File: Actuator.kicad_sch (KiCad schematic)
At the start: 2 parts, among them U4 DRV8833PWPR, U6 DRV8833PWPR

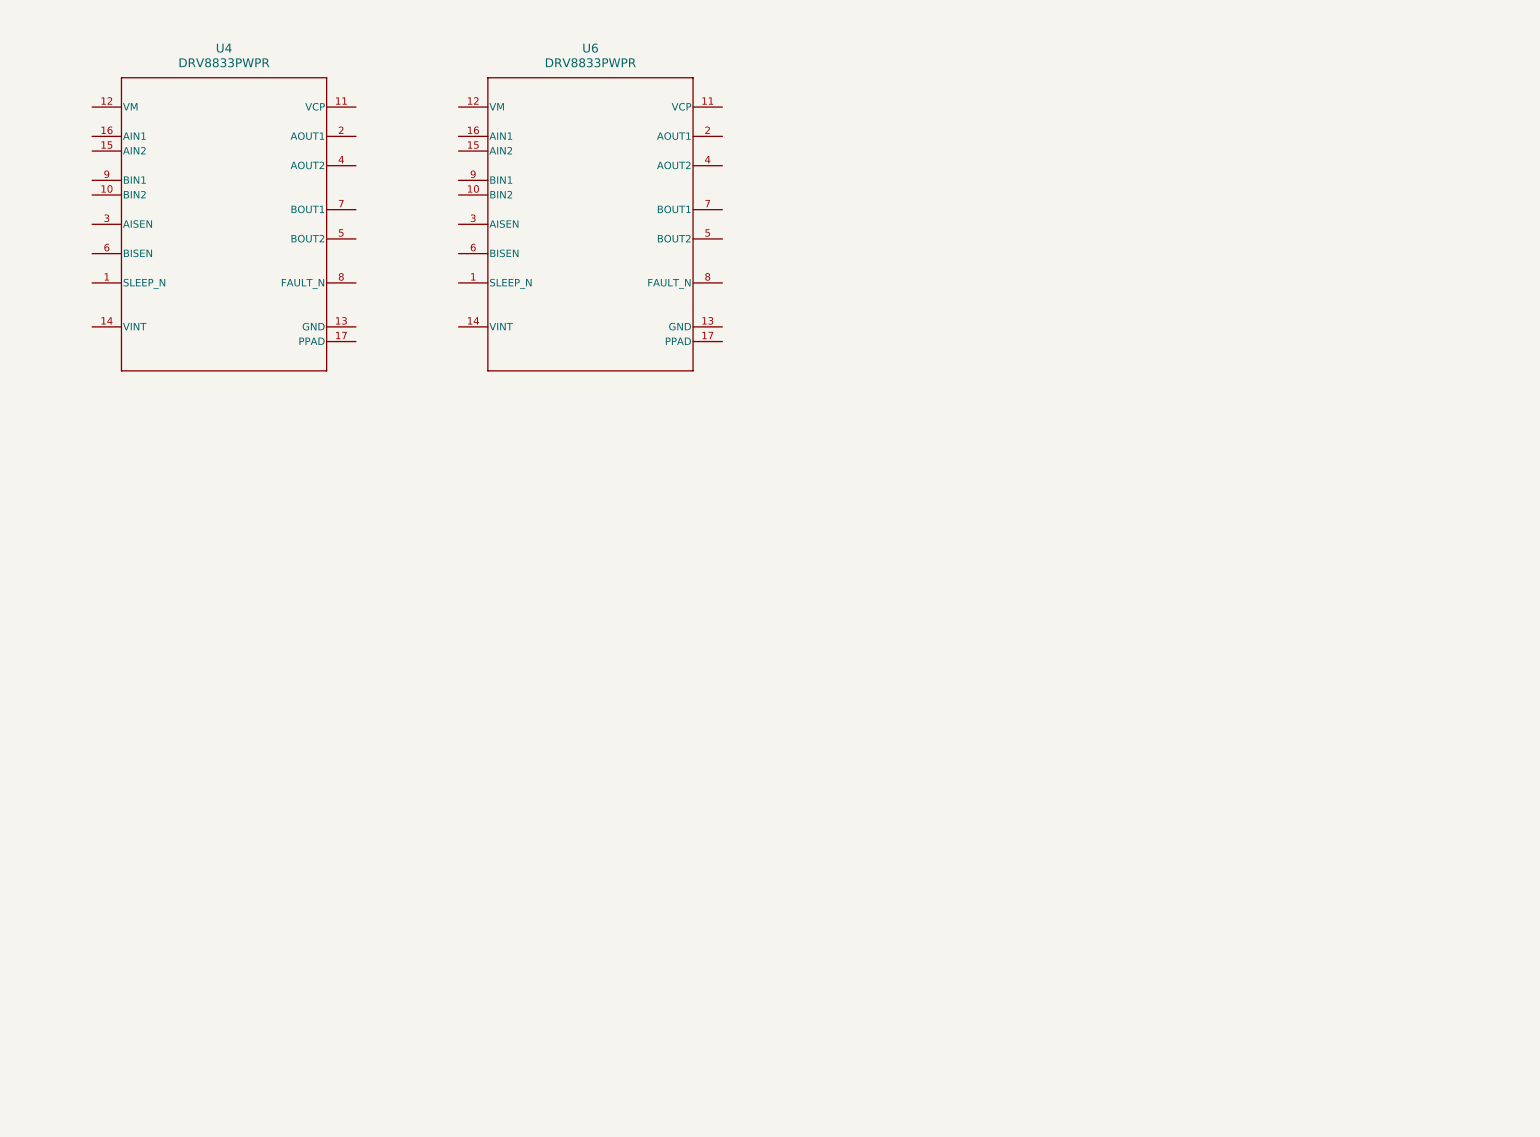
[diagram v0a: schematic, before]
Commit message: Added actuation circuit for x, y, and z axes
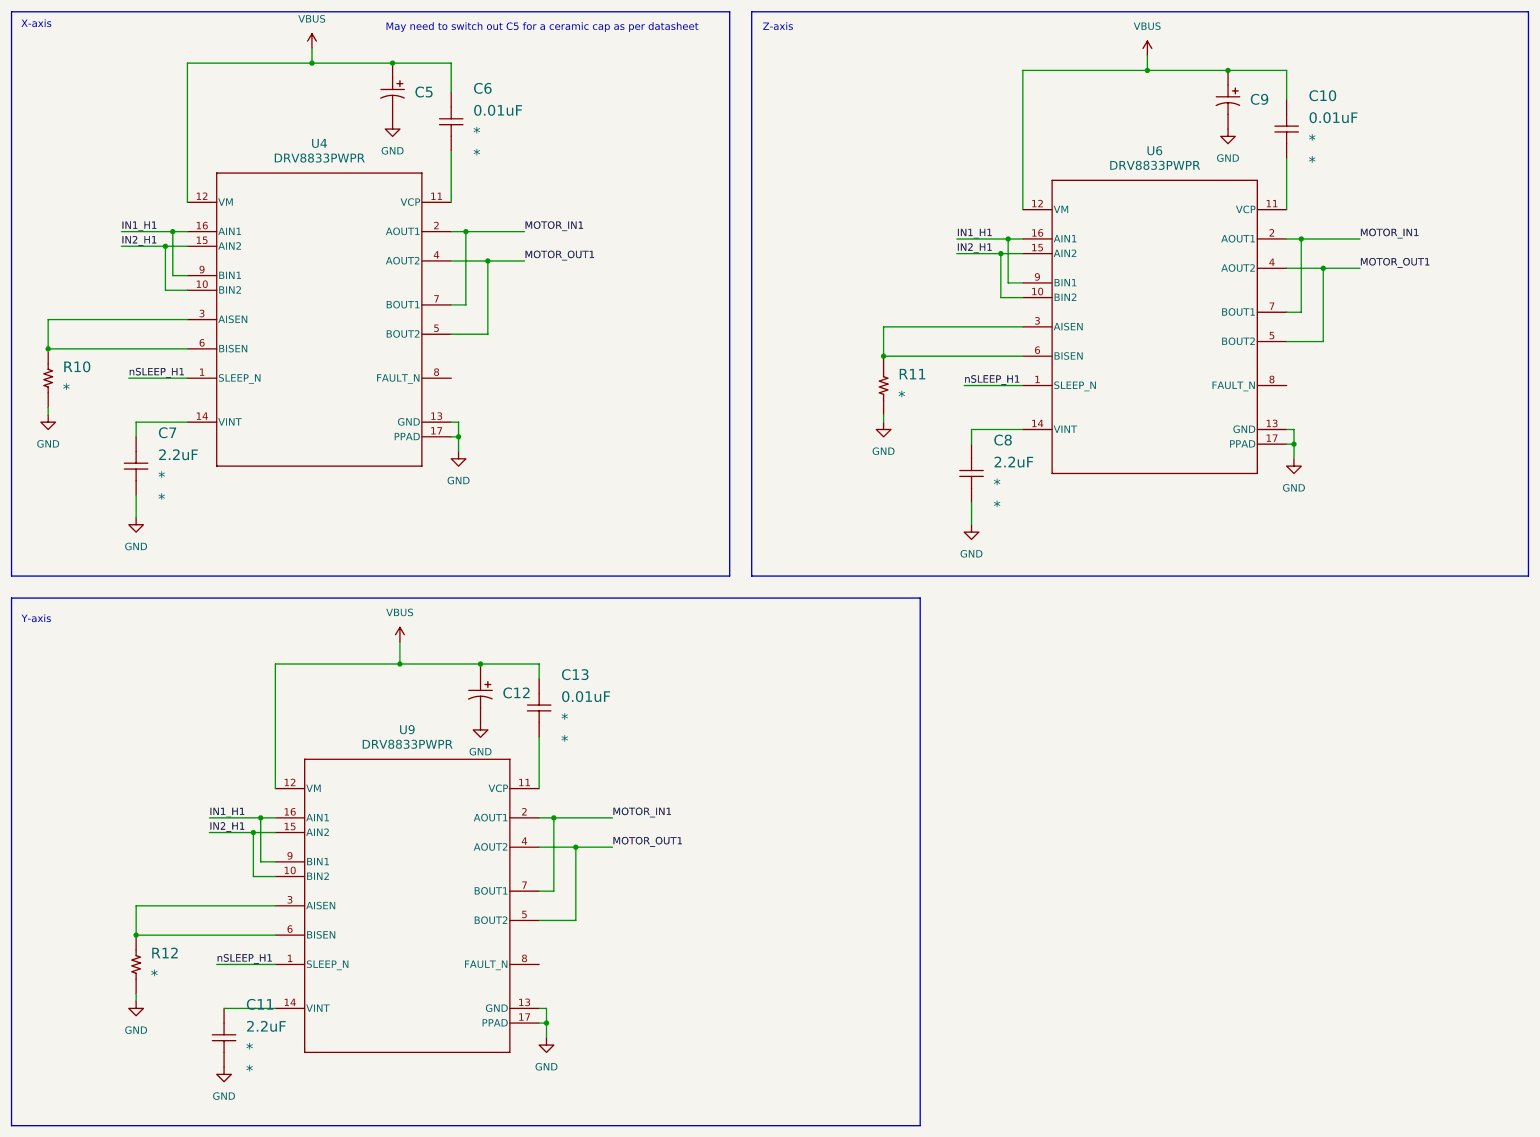
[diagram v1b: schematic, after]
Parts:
- added C10, C13, C6: 0.01uF, symbol Capacitor:Capacitor_NP
- added C11, C7, C8: 2.2uF, symbol Capacitor:Capacitor_NP
- added C12, C5, C9: 10uF, symbol Capacitor:Capacitor_POL
- added R10, R11, R12: *, symbol Resistor:Resistor
- added U9: DRV8833PWPR, Leaded:PWP0016C_N, symbol DB:Power/2601
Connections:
- net nSLEEP_H1: now reaches U6.1 (SLEEP_N)
- net nSLEEP_H1: now also U4.1 (SLEEP_N), U9.1 (SLEEP_N)
- net IN2_H1: now reaches U6.10 (BIN2)
- net IN2_H1: now also U4.10 (BIN2), U4.15 (AIN2), U6.15 (AIN2), U9.10 (BIN2), U9.15 (AIN2)
- net at U6.11 (VCP): now also C10.2
- net VBUS: now reaches U6.12 (VM)
- net VBUS: now also U4.12 (VM), C10.1, C12.1, C13.1, C5.1, C6.1, C9.1, U9.12 (VM)
- net GND: now reaches U6.13 (GND)
- net GND: now also U4.13 (GND), U4.17 (PPAD), U6.17 (PPAD), C11.2, C12.2, C5.2, C7.2, C8.2, C9.2, R10.2, R11.2, R12.2, U9.13 (GND), U9.17 (PPAD)
- net at U6.14 (VINT): now also C8.1
- net IN1_H1: now reaches U6.16 (AIN1)
- net IN1_H1: now also U4.16 (AIN1), U4.9 (BIN1), U6.9 (BIN1), U9.16 (AIN1), U9.9 (BIN1)
- net MOTOR_IN1: now reaches U6.2 (AOUT1)
- net MOTOR_IN1: now also U4.2 (AOUT1), U4.7 (BOUT1), U6.7 (BOUT1), U9.2 (AOUT1), U9.7 (BOUT1)
- net at U6.3 (AISEN): now also U6.6 (BISEN), R11.1
- net MOTOR_OUT1: now reaches U6.4 (AOUT2)
- net MOTOR_OUT1: now also U4.4 (AOUT2), U4.5 (BOUT2), U6.5 (BOUT2), U9.4 (AOUT2), U9.5 (BOUT2)
- net at U4.11 (VCP): now also C6.2
- net at U4.14 (VINT): now also C7.1
- net at U4.3 (AISEN): now also U4.6 (BISEN), R10.1
- new net: C13.2, U9.11 (VCP)
- new net: R12.1, U9.3 (AISEN), U9.6 (BISEN)
- new net: C11.1, U9.14 (VINT)
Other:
- note added: "May need to switch out C5 for a ceramic cap as per datasheet"
- note added: "X-axis"
- note added: "Y-axis"
- note added: "Z-axis"
- moved on the sheet: U4
